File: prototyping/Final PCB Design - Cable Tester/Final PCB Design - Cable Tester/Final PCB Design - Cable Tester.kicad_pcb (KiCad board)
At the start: 2 copper layers, 86 x 54 mm, 41 parts, among them J1 SFML-110-T1-S-D, J17 Banana Jack, J3 Debug Connection, J4 MEM2061-01-188-00-A_REVA, J5 54-00129, J6 Touchscreen HMI, Q1 MMBT3904, SW1 1x2 Pin header, U1 AVR128DB64x-xMR, U2 LP2985-33DBVR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

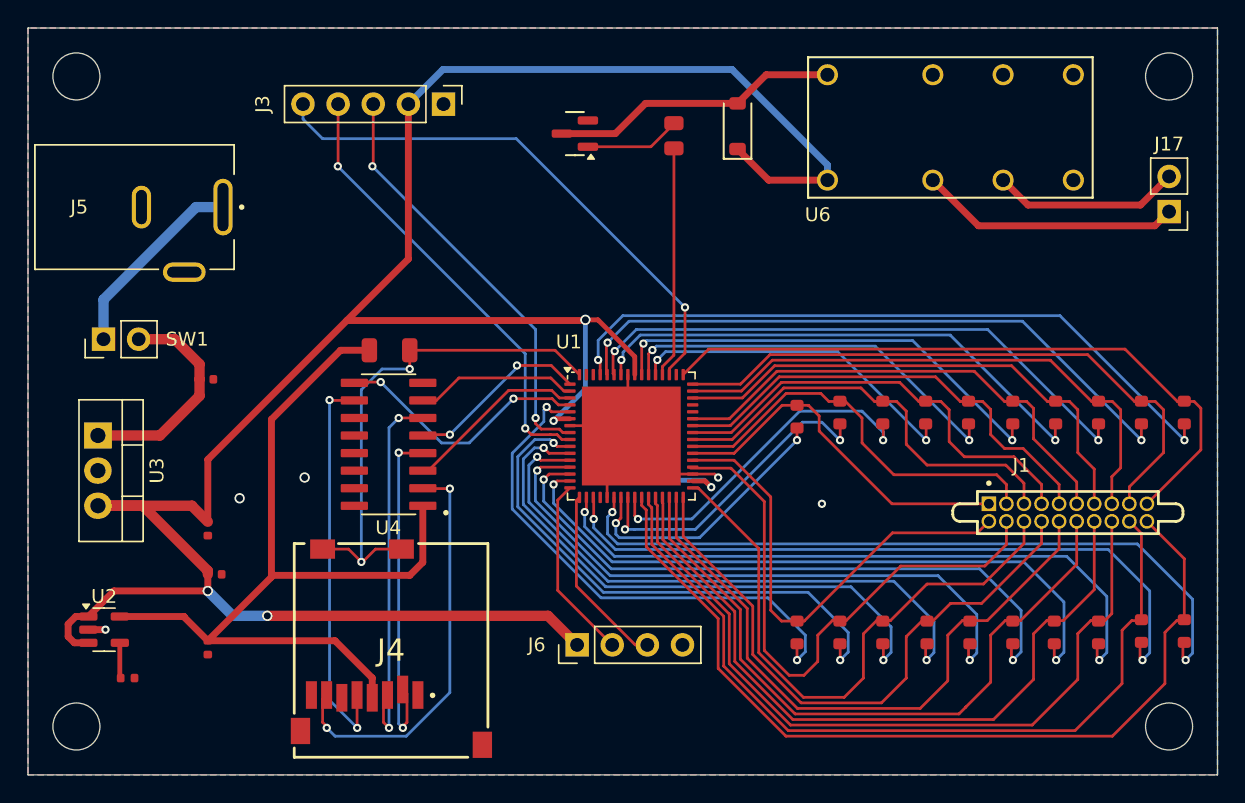
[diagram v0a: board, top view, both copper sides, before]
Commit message: Changes to Final board design
Re-routed the DO from microSD to MCU (No more level shifter), added a 5V line to pin 20 so that port C will be powered. Fixed other minor issues after running DRC on layout design.
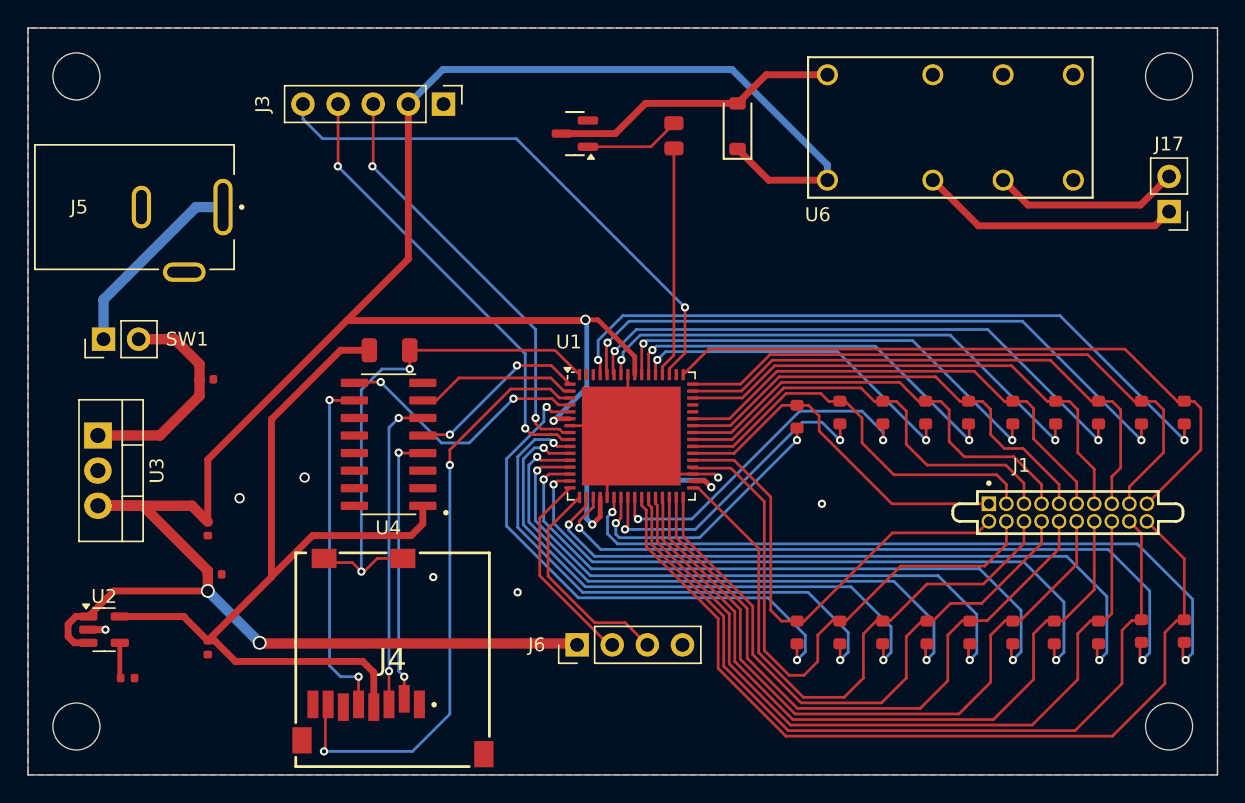
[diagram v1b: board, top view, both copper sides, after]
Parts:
- moved J4 0.68 mm to (117.9, 111.7)
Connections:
- J4 pad 7: /mSD_DO -> DO
- U1 pad 20: unconnected-(U1-VDDIO2-Pad20) -> +5V
- U4 pad 2: /mSD_DO -> unconnected-(U4-1Y-Pad2)
- U4 pad 3: DO -> unconnected-(U4-1A-Pad3)
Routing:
- net DO: track 13.3 -> 43.3 mm, vias 0 -> 2
- net /mSD_DO: track 29.8 -> 0.00 mm, vias 2 -> 0
- net +5V: track 187.0 -> 199.3 mm, vias 5 -> 6
- net /mSD_CS: track 24.8 -> 20.0 mm
- net /mSD_DI: track 27.1 -> 23.0 mm
- net /mSD_CLK: track 28.7 -> 25.7 mm
- net Rx1: track 13.4 -> 15.9 mm
- net CTRL 8: track 48.1 -> 49.9 mm
- net CTRL 9: track 50.8 -> 52.3 mm
- net CTRL 1: track 38.4 -> 39.7 mm
- net Tx1: track 13.3 -> 14.6 mm
- net CTRL 2: track 39.2 -> 40.1 mm
- net CTRL 3: track 41.2 -> 42.1 mm
- net CTRL 6: track 46.5 -> 47.4 mm
- net CTRL 7: track 48.1 -> 49.0 mm
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
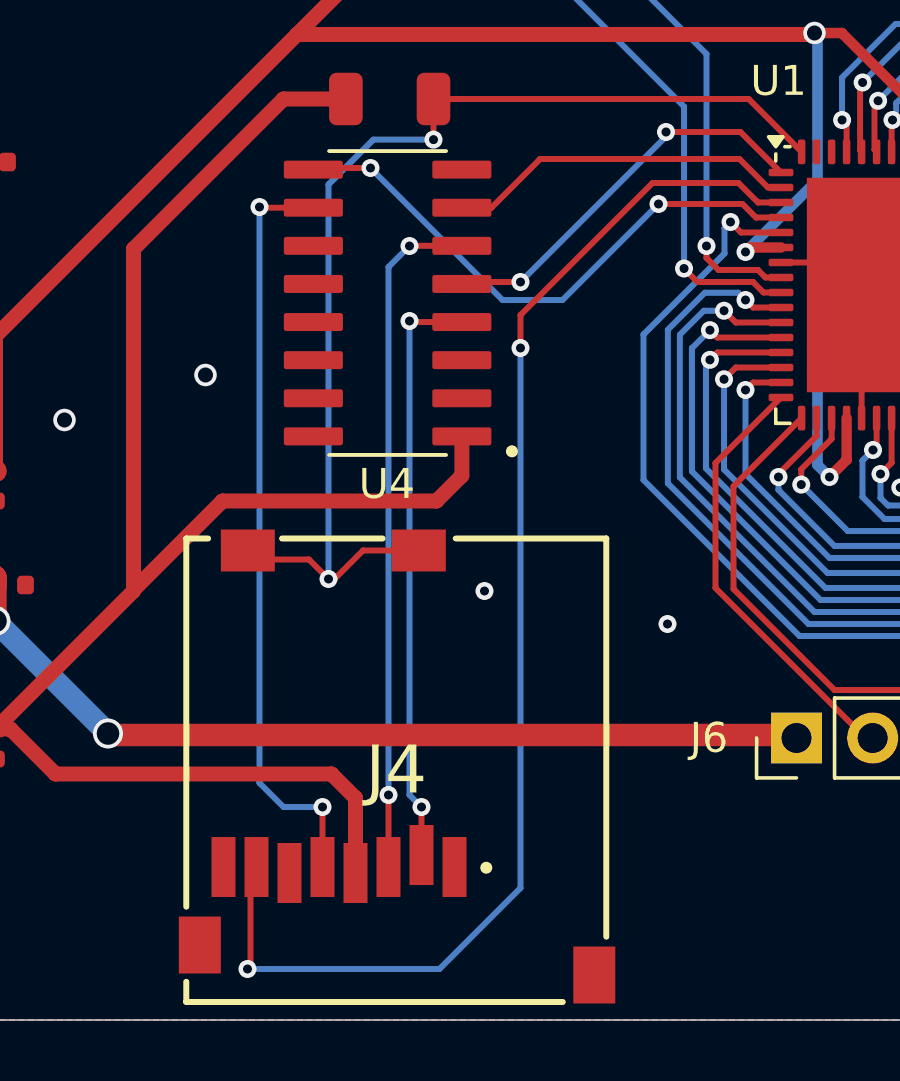
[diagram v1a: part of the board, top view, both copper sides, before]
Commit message: Updated final PCB
Tied pin 3 of U4 to GND. Updated the Gerber files for manufacturing.
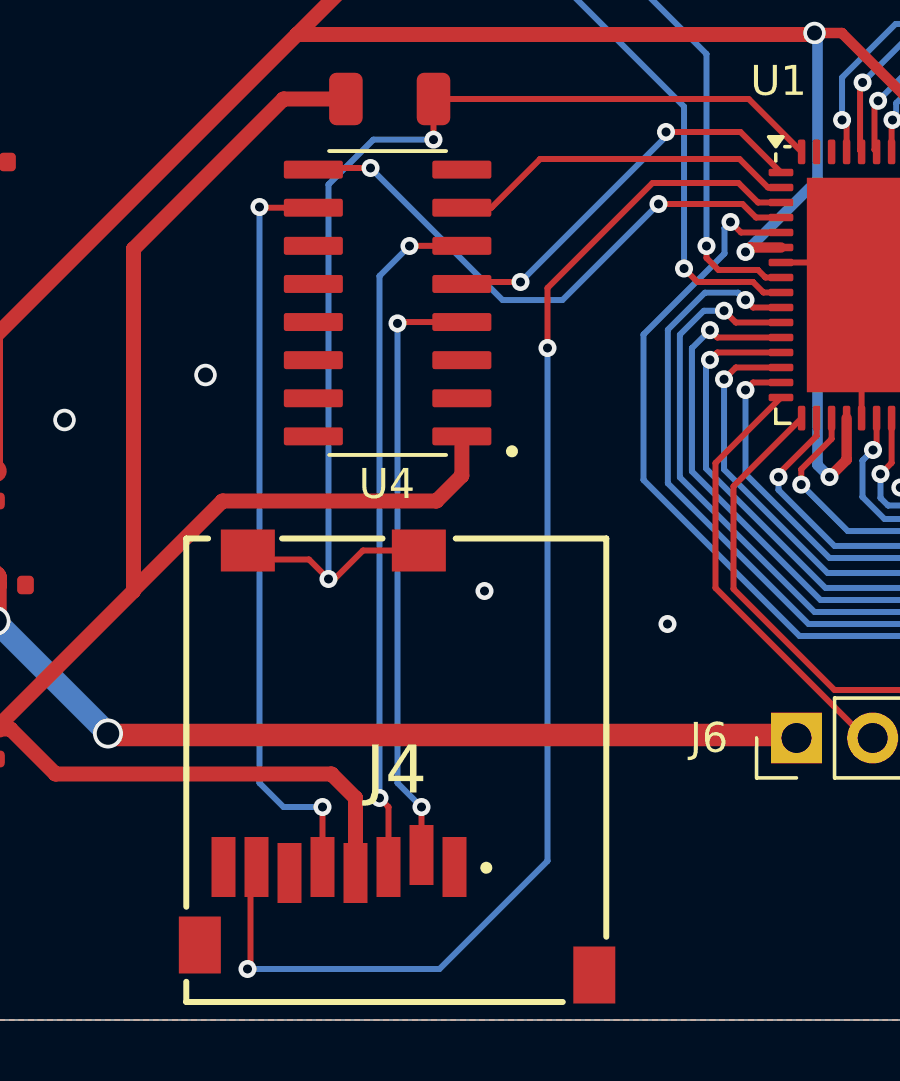
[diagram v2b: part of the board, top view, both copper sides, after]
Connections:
- U4 pad 3: unconnected-(U4-1A-Pad3) -> GND
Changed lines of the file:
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@@
 			(drillshape 0)
 			(scaleselection 1)
-			(outputdirectory "./")
+			(outputdirectory "Gerbers/")
 		)
 	)
@@
 	(net 70 "GND")
 	(net 71 "/mSD_DI")
-	(net 72 "unconnected-(U4-1A-Pad3)")
-	(net 73 "/mSD_CS")
-	(net 74 "/mSD_CLK")
-	(net 75 "Net-(Q1-C)")
-	(net 76 "Net-(Q1-B)")
-	(net 77 "unconnected-(U4-NC_13-Pad13)")
-	(net 78 "unconnected-(U4-6Y-Pad15)")
-	(net 79 "unconnected-(U4-NC_16-Pad16)")
-	(net 80 "unconnected-(U4-5Y-Pad12)")
+	(net 72 "/mSD_CS")
+	(net 73 "/mSD_CLK")
+	(net 74 "Net-(Q1-C)")
+	(net 75 "Net-(Q1-B)")
+	(net 76 "unconnected-(U4-NC_13-Pad13)")
+	(net 77 "unconnected-(U4-6Y-Pad15)")
+	(net 78 "unconnected-(U4-NC_16-Pad16)")
+	(net 79 "unconnected-(U4-5Y-Pad12)")
 	(footprint "PCM_JLCPCB:R_0603"
 		(layer "F.Cu")
@@
 			)
 			(remove_unused_layers no)
-			(net 75 "Net-(Q1-C)")
+			(net 74 "Net-(Q1-C)")
 			(pinfunction "8")
 			(pintype "unspecified")
@@
 			(layers "F.Cu" "F.Mask" "F.Paste")
 			(roundrect_rratio 0.243902)
-			(net 76 "Net-(Q1-B)")
+			(net 75 "Net-(Q1-B)")
 			(pintype "passive")
 		)
@@
 			(size 0.8 2)
 			(layers "F.Cu" "F.Mask" "F.Paste")
-			(net 73 "/mSD_CS")
+			(net 72 "/mSD_CS")
 			(pinfunction "CD/DAT3")
 			(pintype "bidirectional")
@@
 			(size 0.8 2)
 			(layers "F.Cu" "F.Mask" "F.Paste")
-			(net 74 "/mSD_CLK")
+			(net 73 "/mSD_CLK")
 			(pinfunction "CLK")
 			(pintype "bidirectional")
@@
 			(layers "F.Cu" "F.Mask" "F.Paste")
 			(roundrect_rratio 0.25)
-			(net 75 "Net-(Q1-C)")
+			(net 74 "Net-(Q1-C)")
 			(pintype "passive")
 		)
@@
 			(layers "F.Cu" "F.Mask" "F.Paste")
 			(roundrect_rratio 0.125)
-			(net 72 "unconnected-(U4-1A-Pad3)")
+			(net 70 "GND")
 			(pinfunction "1A")
 			(pintype "input")
@@
 			(layers "F.Cu" "F.Mask" "F.Paste")
 			(roundrect_rratio 0.125)
-			(net 73 "/mSD_CS")
+			(net 72 "/mSD_CS")
 			(pinfunction "2Y")
 			(pintype "output")
@@
 			(layers "F.Cu" "F.Mask" "F.Paste")
 			(roundrect_rratio 0.125)
-			(net 74 "/mSD_CLK")
+			(net 73 "/mSD_CLK")
 			(pinfunction "4Y")
 			(pintype "output")
@@
 			(layers "F.Cu" "F.Mask" "F.Paste")
 			(roundrect_rratio 0.125)
-			(net 80 "unconnected-(U4-5Y-Pad12)")
+			(net 79 "unconnected-(U4-5Y-Pad12)")
 			(pinfunction "5Y")
 			(pintype "output+no_connect")
@@
 			(layers "F.Cu" "F.Mask" "F.Paste")
 			(roundrect_rratio 0.125)
-			(net 77 "unconnected-(U4-NC_13-Pad13)")
+			(net 76 "unconnected-(U4-NC_13-Pad13)")
 			(pinfunction "NC_13")
 			(pintype "passive+no_connect")
@@
 			(layers "F.Cu" "F.Mask" "F.Paste")
 			(roundrect_rratio 0.125)
-			(net 78 "unconnected-(U4-6Y-Pad15)")
+			(net 77 "unconnected-(U4-6Y-Pad15)")
 			(pinfunction "6Y")
 			(pintype "output+no_connect")
@@
 			(layers "F.Cu" "F.Mask" "F.Paste")
 			(roundrect_rratio 0.125)
-			(net 79 "unconnected-(U4-NC_16-Pad16)")
+			(net 78 "unconnected-(U4-NC_16-Pad16)")
 			(pinfunction "NC_16")
 			(pintype "passive+no_connect")
@@
 			(layers "F.Cu" "F.Mask" "F.Paste")
 			(roundrect_rratio 0.25)
-			(net 76 "Net-(Q1-B)")
+			(net 75 "Net-(Q1-B)")
 			(pinfunction "B")
 			(pintype "input")
@@
 			(layers "F.Cu" "F.Mask" "F.Paste")
 			(roundrect_rratio 0.25)
-			(net 75 "Net-(Q1-C)")
+			(net 74 "Net-(Q1-C)")
 			(pinfunction "C")
 			(pintype "open_collector")
@@
 	)
 	(segment
-		(start 129.267043 92.1)
-		(end 129.917043 92.75)
+		(start 122.9 95.6)
+		(end 126.4 92.1)
 		(width 0.2)
 		(layer "F.Cu")
@@
 	)
 	(segment
-		(start 122 97.6)
-		(end 122 96.5)
+		(start 112.9 118.3)
+		(end 113 118.2)
 		(width 0.2)
 		(layer "F.Cu")
@@
 	)
 	(segment
-		(start 112.9 118.3)
-		(end 113 118.2)
+		(start 129.267043 92.1)
+		(end 129.917043 92.75)
 		(width 0.2)
 		(layer "F.Cu")
@@
 	)
 	(segment
-		(start 122 96.5)
-		(end 126.4 92.1)
+		(start 129.917043 92.75)
+		(end 130.6825 92.75)
 		(width 0.2)
 		(layer "F.Cu")
@@
 	)
 	(segment
-		(start 113 118.2)
-		(end 113 115.4)
+		(start 122.9 97.6)
+		(end 122.9 95.6)
 		(width 0.2)
 		(layer "F.Cu")
@@
 	)
 	(segment
-		(start 129.917043 92.75)
-		(end 130.6825 92.75)
+		(start 113 118.2)
+		(end 113 115.4)
 		(width 0.2)
 		(layer "F.Cu")
@@
 	)
 	(via
-		(at 122 97.6)
+		(at 122.9 97.6)
 		(size 0.6)
 		(drill 0.3)
@@
 	)
 	(segment
-		(start 122 115.6)
-		(end 122 97.6)
+		(start 122.9 114.7)
+		(end 119.3 118.3)
 		(width 0.2)
 		(layer "B.Cu")
@@
 	)
 	(segment
-		(start 119.3 118.3)
-		(end 122 115.6)
+		(start 122.9 97.6)
+		(end 122.9 114.7)
 		(width 0.2)
 		(layer "B.Cu")
@@
 	)
 	(segment
-		(start 112.9 118.3)
-		(end 119.3 118.3)
+		(start 119.3 118.3)
+		(end 112.9 118.3)
 		(width 0.2)
 		(layer "B.Cu")
@@
 	)
 	(segment
-		(start 117.6 112.5)
+		(start 117.6 112.9)
 		(end 117.6 115.2)
 		(width 0.2)
@@
 	)
 	(segment
+		(start 117.3 112.6)
+		(end 117.6 112.9)
+		(width 0.2)
+		(layer "F.Cu")
+		(net 71)
+	)
+	(segment
 		(start 120.045 94.195)
 		(end 118.305 94.195)
@@
 	)
 	(via
-		(at 117.6 112.5)
+		(at 117.3 112.6)
 		(size 0.6)
 		(drill 0.3)
@@
 	)
 	(segment
-		(start 117.6 94.9)
-		(end 118.3 94.2)
+		(start 117.3 112.6)
+		(end 117.3 95.2)
 		(width 0.2)
 		(layer "B.Cu")
@@
 	)
 	(segment
-		(start 117.6 112.5)
-		(end 117.6 94.9)
+		(start 117.3 95.2)
+		(end 118.3 94.2)
 		(width 0.2)
 		(layer "B.Cu")
@@
 	)
 	(segment
-		(start 120.045 96.735)
-		(end 118.335 96.735)
+		(start 117.9 96.778974)
+		(end 117.943974 96.735)
 		(width 0.2)
 		(layer "F.Cu")
-		(net 73)
+		(net 72)
 	)
 	(segment
-		(start 118.7 112.9)
-		(end 118.7 114.8)
+		(start 117.943974 96.735)
+		(end 120.045 96.735)
 		(width 0.2)
 		(layer "F.Cu")
-		(net 73)
+		(net 72)
 	)
 	(segment
-		(start 118.335 96.735)
-		(end 118.3 96.7)
+		(start 118.7 112.9)
+		(end 118.7 114.8)
 		(width 0.2)
 		(layer "F.Cu")
-		(net 73)
+		(net 72)
 	)
 	(via
-		(at 118.3 96.7)
+		(at 117.9 96.778974)
 		(size 0.6)
 		(drill 0.3)
 		(layers "F.Cu" "B.Cu")
 		(free yes)
-		(net 73)
+		(net 72)
 	)
 	(via
@@
 		(layers "F.Cu" "B.Cu")
 		(free yes)
-		(net 73)
+		(net 72)
 	)
 	(segment
-		(start 118.3 112.5)
-		(end 118.3 96.7)
+		(start 117.9 112.1)
+		(end 118.7 112.9)
 		(width 0.2)
 		(layer "B.Cu")
-		(net 73)
+		(net 72)
 	)
 	(segment
-		(start 118.7 112.9)
-		(end 118.3 112.5)
+		(start 117.9 96.778974)
+		(end 117.9 112.1)
 		(width 0.2)
 		(layer "B.Cu")
-		(net 73)
+		(net 72)
 	)
 	(segment
@@
 		(width 0.2)
 		(layer "F.Cu")
-		(net 74)
+		(net 73)
 	)
 	(segment
@@
 		(width 0.2)
 		(layer "F.Cu")
-		(net 74)
+		(net 73)
 	)
 	(segment
@@
 		(width 0.2)
 		(layer "F.Cu")
-		(net 74)
+		(net 73)
 	)
 	(via
@@
 		(layers "F.Cu" "B.Cu")
 		(free yes)
-		(net 74)
+		(net 73)
 	)
 	(via
@@
 		(layers "F.Cu" "B.Cu")
 		(free yes)
-		(net 74)
+		(net 73)
 	)
 	(segment
@@
 		(width 0.2)
 		(layer "B.Cu")
-		(net 74)
+		(net 73)
 	)
 	(segment
@@
 		(width 0.2)
 		(layer "B.Cu")
-		(net 74)
+		(net 73)
 	)
 	(segment
@@
 		(width 0.2)
 		(layer "B.Cu")
-		(net 74)
+		(net 73)
 	)
 	(segment
@@
 		(width 0.5)
 		(layer "F.Cu")
-		(net 75)
+		(net 74)
 	)
 	(segment
@@
 		(width 0.5)
 		(layer "F.Cu")
-		(net 75)
+		(net 74)
 	)
 	(segment
@@
 		(width 0.5)
 		(layer "F.Cu")
-		(net 75)
+		(net 74)
 	)
 	(segment
@@
 		(width 0.5)
 		(layer "F.Cu")
-		(net 75)
+		(net 74)
 	)
 	(segment
@@
 		(width 0.5)
 		(layer "F.Cu")
-		(net 75)
+		(net 74)
 	)
 	(segment
@@
 		(width 0.2)
 		(layer "F.Cu")
-		(net 76)
+		(net 75)
 	)
 	(segment
@@
 		(width 0.2)
 		(layer "F.Cu")
-		(net 76)
+		(net 75)
 	)
 	(zone
